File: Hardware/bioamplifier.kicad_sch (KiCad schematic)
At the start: 34 parts, among them J1 Conn_01x07_Socket, J3 Conn_01x07_Socket, U1 ADS1299IPAG

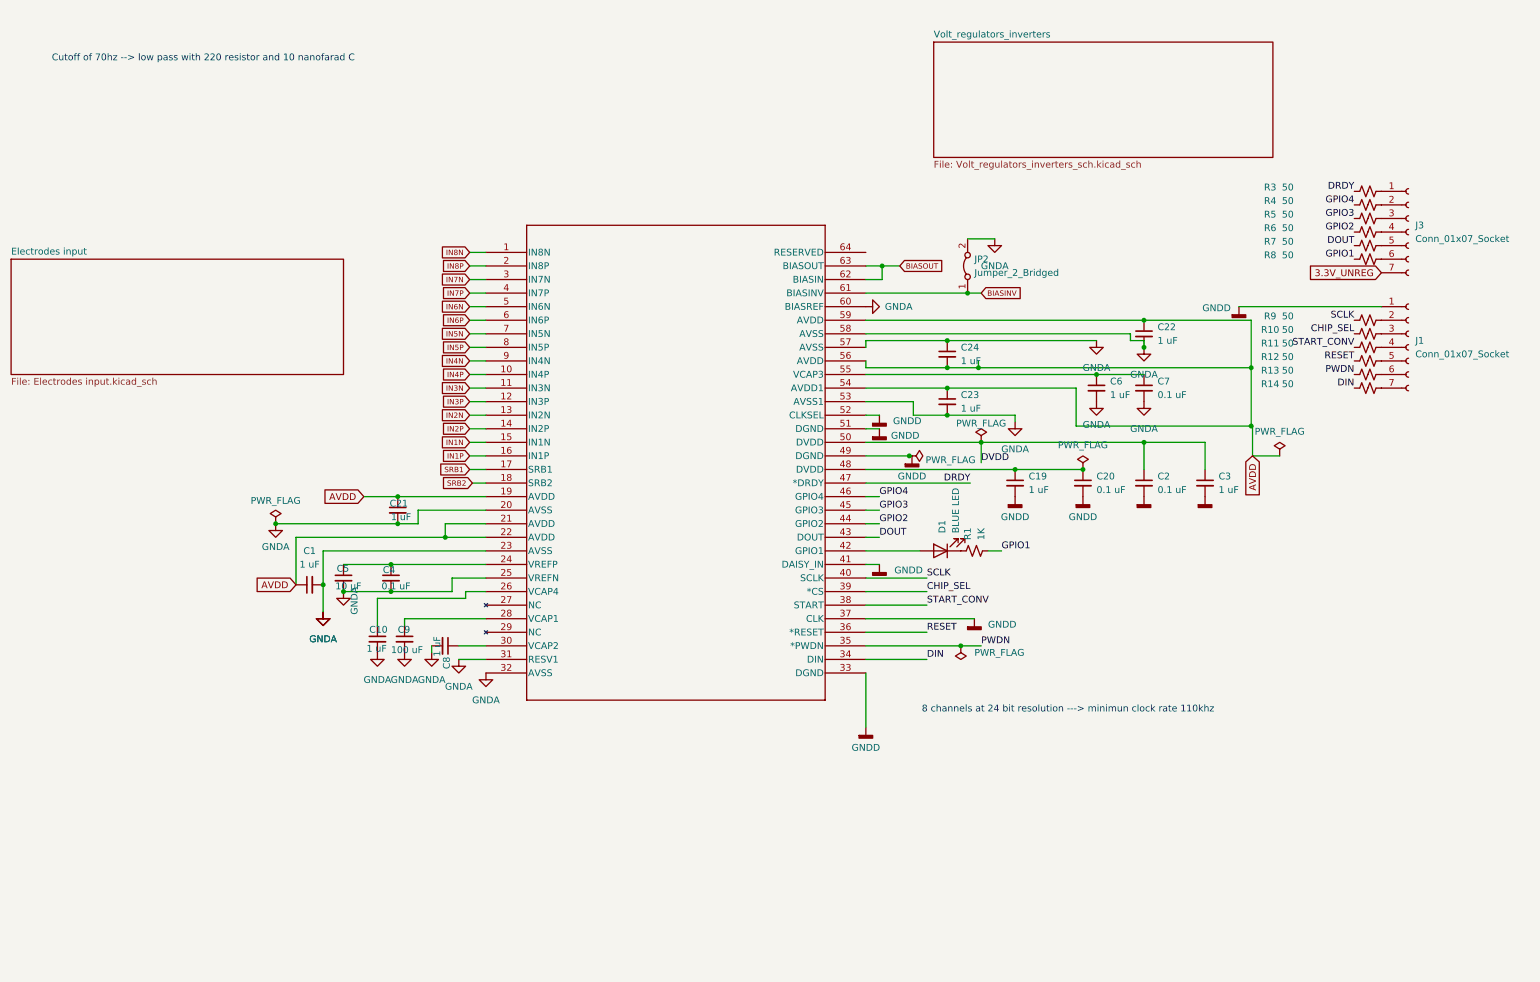
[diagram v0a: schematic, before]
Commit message: power pin layout change
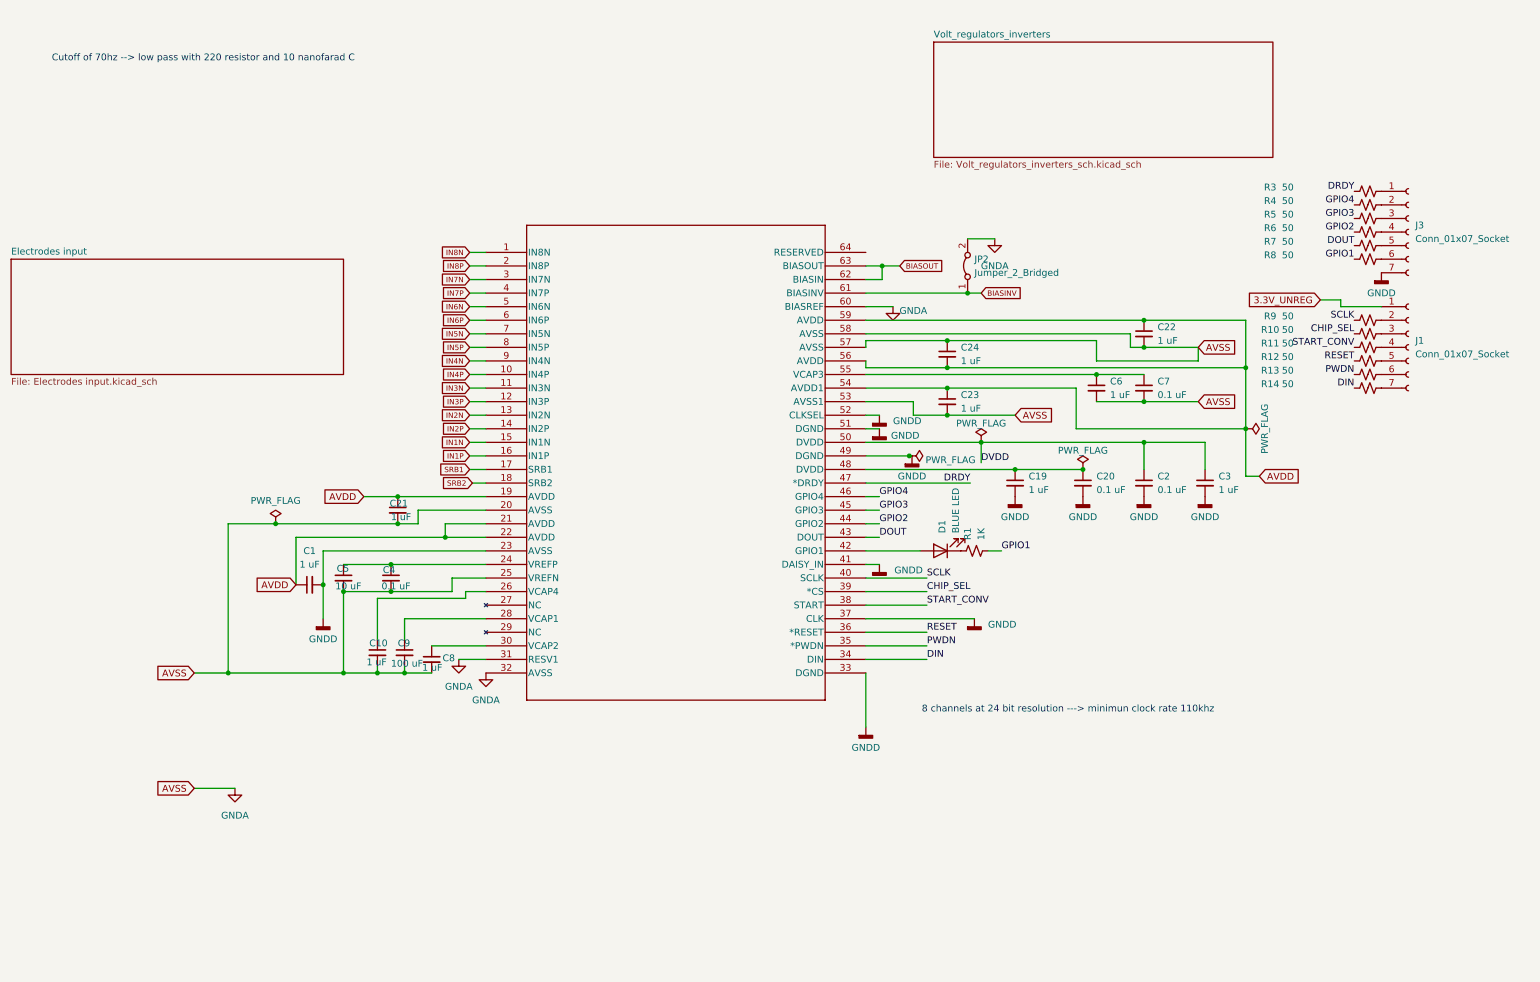
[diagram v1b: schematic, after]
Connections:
- net 3.3V_UNREG: now also J1.1 (Pin_1); no longer J3.7 (Pin_7)
- net GNDA: no longer C1.2, U1.23 (AVSS)
- net GNDD: now also C1.2, J3.7 (Pin_7), U1.23 (AVSS); no longer J1.1 (Pin_1)
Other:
- moved on the sheet: C10, C8, C9

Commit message: Fix Last DRC Errors
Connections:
- net GNDA: no longer C10.2, C21.2, C22.2, C23.2, C24.1, C4.2, C5.2, C6.2, C7.2, C8.2, C9.2, U1.20 (AVSS), U1.25 (VREFN), U1.32 (AVSS), U1.53 (AVSS1), U1.57 (AVSS), U1.58 (AVSS)
- new net AVSS: C10.2, C21.2, C22.2, C23.2, C24.1, C4.2, C5.2, C6.2, C7.2, C8.2, C9.2, U1.20 (AVSS), U1.25 (VREFN), U1.32 (AVSS), U1.53 (AVSS1), U1.57 (AVSS), U1.58 (AVSS)

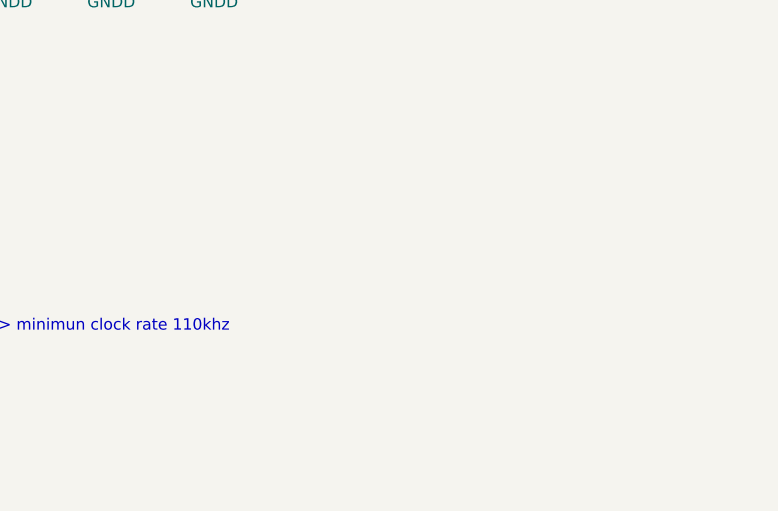
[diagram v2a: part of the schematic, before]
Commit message: Add Fiducials, Mounting holes, 3d models
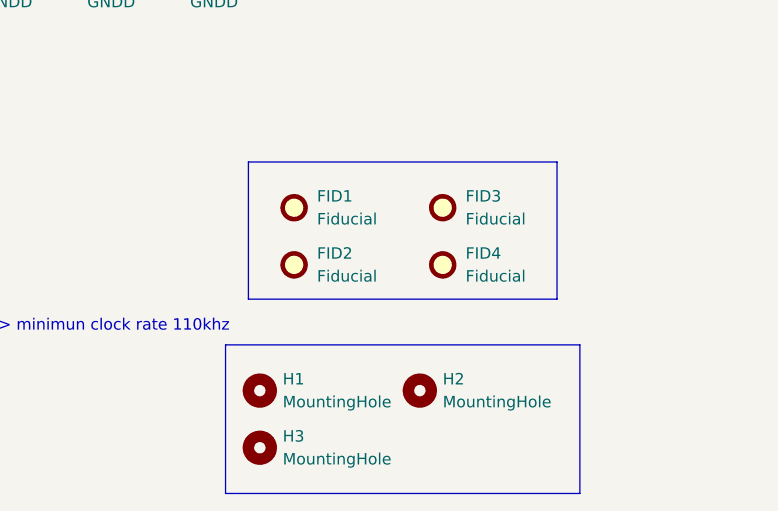
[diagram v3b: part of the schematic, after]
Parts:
- added FID1, FID2, FID3, FID4: Fiducial, Fiducial:Fiducial_1mm_Mask3mm, symbol Mechanical:Fiducial
- added H1, H2, H3: MountingHole, MountingHole:MountingHole_2mm, symbol Mechanical:MountingHole

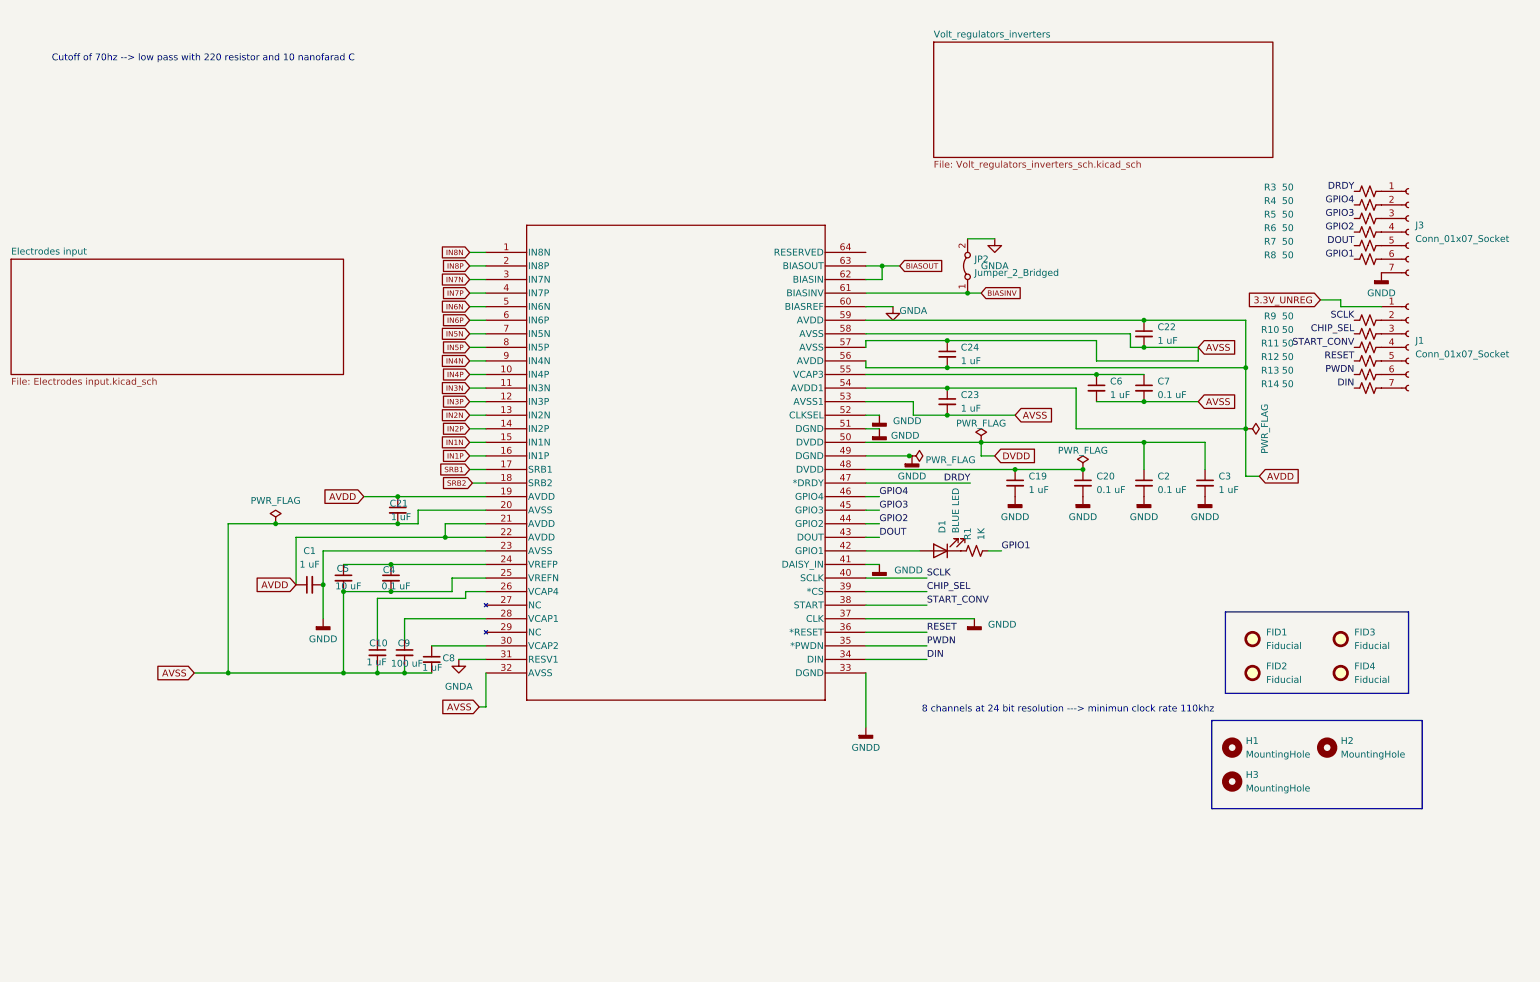
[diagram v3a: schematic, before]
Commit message: Remove redundant components
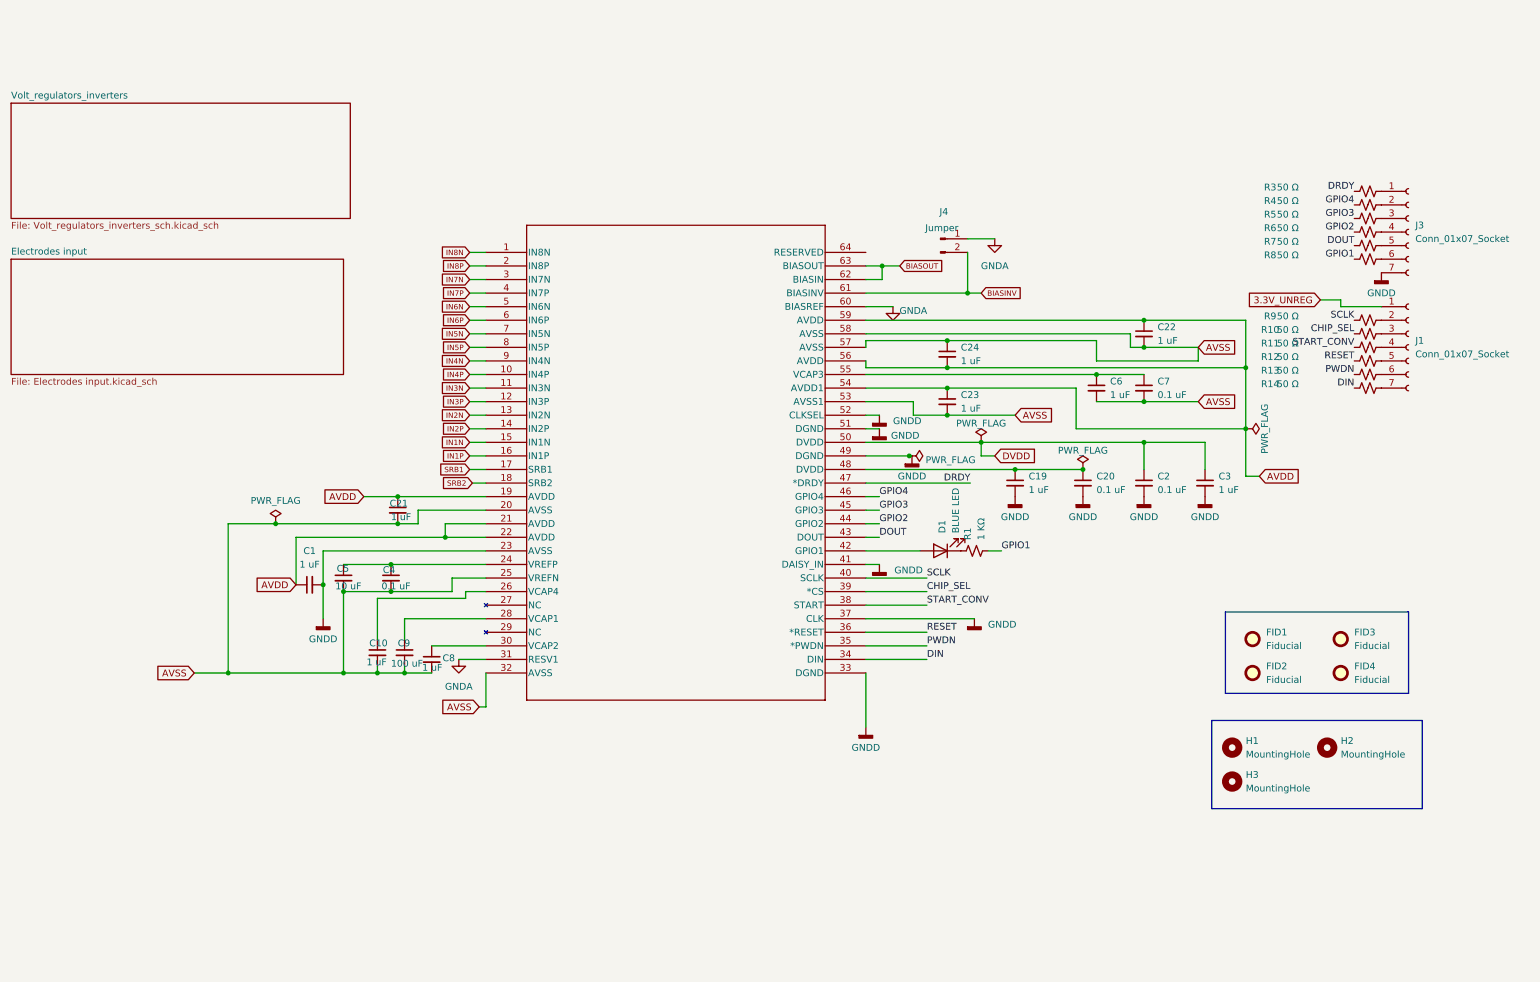
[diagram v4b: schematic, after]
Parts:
- removed JP2: Jumper_2_Bridged, Jumper:SolderJumper-2_P1.3mm_Bridged2Bar_Pad1.0x1.5mm, symbol Jumper:Jumper_2_Bridged
- added J4: Jumper, Connector_PinHeader_2.00mm:PinHeader_1x02_P2.00mm_Vertical, symbol Connector:Conn_01x02_Pin
- R1: value 1K -> 1 KΩ
- R10, R11, R12, R13, R14, R3, R4, R5, R6, R7, R8, R9: value 50 -> 50 Ω
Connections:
- net BIASINV: now also J4.2 (Pin_2)
- net GNDA: now also J4.1 (Pin_1)
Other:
- note removed: "8 channels at 24 bit resolution ---> minimun clock rate 110khz"
- note removed: "Cutoff of 70hz --> low pass with 220 resistor and 10 nanofarad C"
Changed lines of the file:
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@@
 		)
 	)
-	(text "Cutoff of 70hz --> low pass with 220 resistor and 10 nanofarad C\n"
-		(exclude_from_sim no)
-		(at 26.67 25.4 0)
-		(effects
-			(font
-				(size 1.27 1.27)
-			)
-			(justify left bottom)
-		)
-	)
-	(text "8 channels at 24 bit resolution ---> minimun clock rate 110khz\n"
-		(exclude_from_sim no)
-		(at 216.916 146.558 0)
-		(effects
-			(font
-				(size 1.27 1.27)
-			)
-		)
-	)
 	(junction
 		(at 92.71 139.7)
@@
 	)
 	(junction
-		(at 198.12 68.58)
+		(at 77.47 123.19)
 		(diameter 0)
 		(color 0 0 0 0)
 	)
 	(junction
-		(at 77.47 123.19)
+		(at 198.12 68.58)
 		(diameter 0)
 		(color 0 0 0 0)
@@
 	(wire
 		(pts
-			(xy 198.12 68.58) (xy 200.66 68.58)
-		)
-		(stroke
-			(width 0)
-			(type default)
-		)
-	)
-	(wire
-		(pts
 			(xy 87.63 139.7) (xy 87.63 138.43)
 		)
@@
 	(wire
 		(pts
+			(xy 198.12 68.58) (xy 200.66 68.58)
+		)
+		(stroke
+			(width 0)
+			(type default)
+		)
+	)
+	(wire
+		(pts
 			(xy 187.96 91.44) (xy 187.96 88.9)
 		)
@@
 	(wire
 		(pts
+			(xy 198.12 60.96) (xy 198.12 68.58)
+		)
+		(stroke
+			(width 0)
+			(type default)
+		)
+	)
+	(wire
+		(pts
 			(xy 81.28 124.46) (xy 81.28 139.7)
 		)
@@
 			)
 		)
-		(property "Value" "50"
+		(property "Value" "50 Ω"
 			(at 258.064 48.768 90)
 			(effects
@@
 			)
 		)
-		(property "Value" "50"
+		(property "Value" "50 Ω"
 			(at 258.064 58.928 90)
 			(effects
@@
 			)
 		)
-		(property "Value" "50"
+		(property "Value" "50 Ω"
 			(at 258.064 75.438 90)
 			(effects
@@
 			)
 		)
-		(property "Value" "50"
+		(property "Value" "50 Ω"
 			(at 258.064 77.978 90)
 			(effects
@@
 			)
 		)
-		(property "Value" "50"
+		(property "Value" "50 Ω"
 			(at 258.064 80.518 90)
 			(effects
@@
 			)
 		)
-		(property "Value" "50"
+		(property "Value" "50 Ω"
 			(at 258.064 72.898 90)
 			(effects
@@
 			)
 		)
-		(property "Value" "50"
+		(property "Value" "50 Ω"
 			(at 258.064 83.058 90)
 			(effects
@@
 			)
 		)
-		(property "Value" "1K"
+		(property "Value" "1 KΩ"
 			(at 200.66 114.808 0)
 			(effects
@@
 			)
 		)
-		(property "Value" "50"
+		(property "Value" "50 Ω"
 			(at 258.064 51.308 90)
 			(effects
@@
 			)
 		)
-		(property "Value" "50"
+		(property "Value" "50 Ω"
 			(at 258.064 85.598 90)
+			(do_not_autoplace yes)
 			(effects
 				(font
@@
 	)
 	(symbol
-		(lib_id "Jumper:Jumper_2_Bridged")
-		(at 198.12 63.5 90)
-		(unit 1)
-		(exclude_from_sim no)
-		(in_bom yes)
-		(on_board yes)
-		(dnp no)
-		(fields_autoplaced yes)
-		(property "Reference" "JP2"
-			(at 199.39 62.23 90)
-			(effects
-				(font
-					(size 1.27 1.27)
-				)
-				(justify right)
-			)
-		)
-		(property "Value" "Jumper_2_Bridged"
-			(at 199.39 64.77 90)
-			(effects
-				(font
-					(size 1.27 1.27)
-				)
-				(justify right)
-			)
-		)
-		(property "Footprint" "Jumper:SolderJumper-2_P1.3mm_Bridged2Bar_Pad1.0x1.5mm"
-			(at 198.12 63.5 0)
-			(effects
-				(font
-					(size 1.27 1.27)
-				)
-				(hide yes)
-			)
-		)
-		(property "Datasheet" "~"
-			(at 198.12 63.5 0)
-			(effects
-				(font
-					(size 1.27 1.27)
-				)
-				(hide yes)
-			)
-		)
-		(property "Description" ""
-			(at 198.12 63.5 0)
-			(effects
-				(font
-					(size 1.27 1.27)
-				)
-				(hide yes)
-			)
-		)
-		(pin "1"
-		)
-		(pin "2"
-		)
-		(instances
-			(project "bioamplifier"
-				(path "/59c54cdb-19a2-4654-a4c9-f1907d038780"
-					(reference "JP2")
-					(unit 1)
-				)
-			)
-		)
-	)
-	(symbol
 		(lib_id "Mechanical:MountingHole")
 		(at 265.43 153.67 0)
@@
 			)
 		)
-		(property "Value" "50"
+		(property "Value" "50 Ω"
 			(at 258.064 61.468 90)
 			(effects
@@
 	)
 	(symbol
+		(lib_id "Connector:Conn_01x02_Pin")
+		(at 193.04 58.42 0)
+		(unit 1)
+		(exclude_from_sim no)
+		(in_bom yes)
+		(on_board yes)
+		(dnp no)
+		(property "Reference" "J4"
+			(at 193.675 53.34 0)
+			(effects
+				(font
+					(size 1.27 1.27)
+				)
+			)
+		)
+		(property "Value" "Jumper"
+			(at 193.294 56.388 0)
+			(effects
+				(font
+					(size 1.27 1.27)
+				)
+			)
+		)
+		(property "Footprint" "Connector_PinHeader_2.00mm:PinHeader_1x02_P2.00mm_Vertical"
+			(at 193.04 58.42 0)
+			(effects
+				(font
+					(size 1.27 1.27)
+				)
+				(hide yes)
+			)
+		)
+		(property "Datasheet" "~"
+			(at 193.04 58.42 0)
+			(effects
+				(font
+					(size 1.27 1.27)
+				)
+				(hide yes)
+			)
+		)
+		(property "Description" "Generic connector, single row, 01x02, script generated"
+			(at 193.04 58.42 0)
+			(effects
+				(font
+					(size 1.27 1.27)
+				)
+				(hide yes)
+			)
+		)
+		(pin "2"
+		)
+		(pin "1"
+		)
+		(instances
+			(project ""
+				(path "/59c54cdb-19a2-4654-a4c9-f1907d038780"
+					(reference "J4")
+					(unit 1)
+				)
+			)
+		)
+	)
+	(symbol
 		(lib_id "Device:C_Small")
 		(at 81.28 121.92 0)
@@
 			)
 		)
-		(property "Value" "50"
+		(property "Value" "50 Ω"
 			(at 258.064 56.388 90)
 			(effects
@@
 			)
 		)
-		(property "Value" "50"
+		(property "Value" "50 Ω"
 			(at 258.064 53.848 90)
 			(effects
@@
 	)
 	(sheet
-		(at 191.77 21.59)
+		(at 19.05 33.02)
 		(size 63.5 21.59)
 		(exclude_from_sim no)
@@
 		)
 		(property "Sheetname" "Volt_regulators_inverters"
-			(at 191.77 20.8784 0)
+			(at 19.05 32.3084 0)
 			(effects
 				(font
@@
 		)
 		(property "Sheetfile" "Volt_regulators_inverters_sch.kicad_sch"
-			(at 191.77 43.7646 0)
+			(at 19.05 55.1946 0)
 			(effects
 				(font
@@
 		)
 		(property "Field2" ""
-			(at 191.77 21.59 0)
+			(at 19.05 33.02 0)
 			(effects
 				(font
